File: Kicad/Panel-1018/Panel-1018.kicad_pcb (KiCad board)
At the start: 2 copper layers, 100 x 100 mm, 60 parts, among them P1 CONN2X3MOLEX, P10 CONN_6, P11 TST, P12 TST, P13 TST, P14 TST, P15 TST, P16 TST, P4 TST, P7 TST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

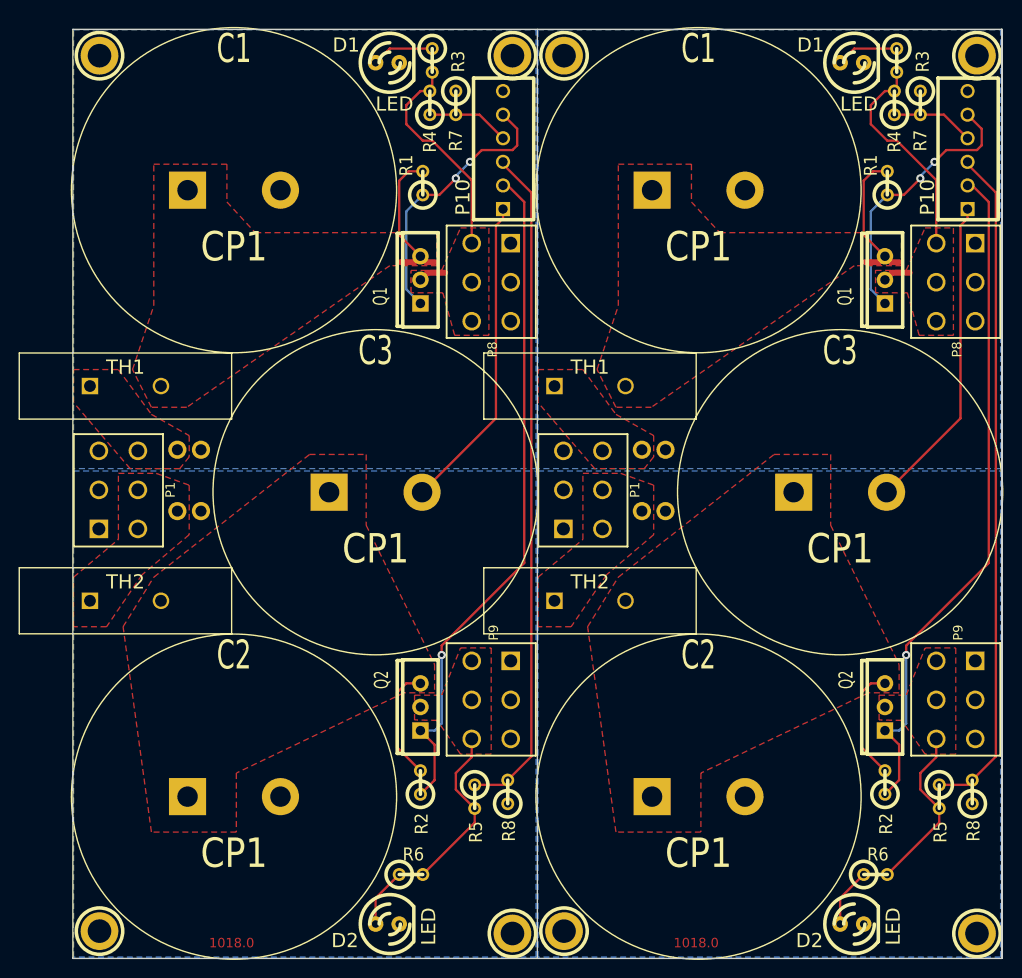
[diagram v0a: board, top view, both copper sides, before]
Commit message: Kicad:  Rename Panel-1018/Gerber/Gerber.zip to Panel-1018.zip.  Fix title on PCB legend.  Create Panel-1019 and Panel-1020 to panelize solenoid and incandescent planks.
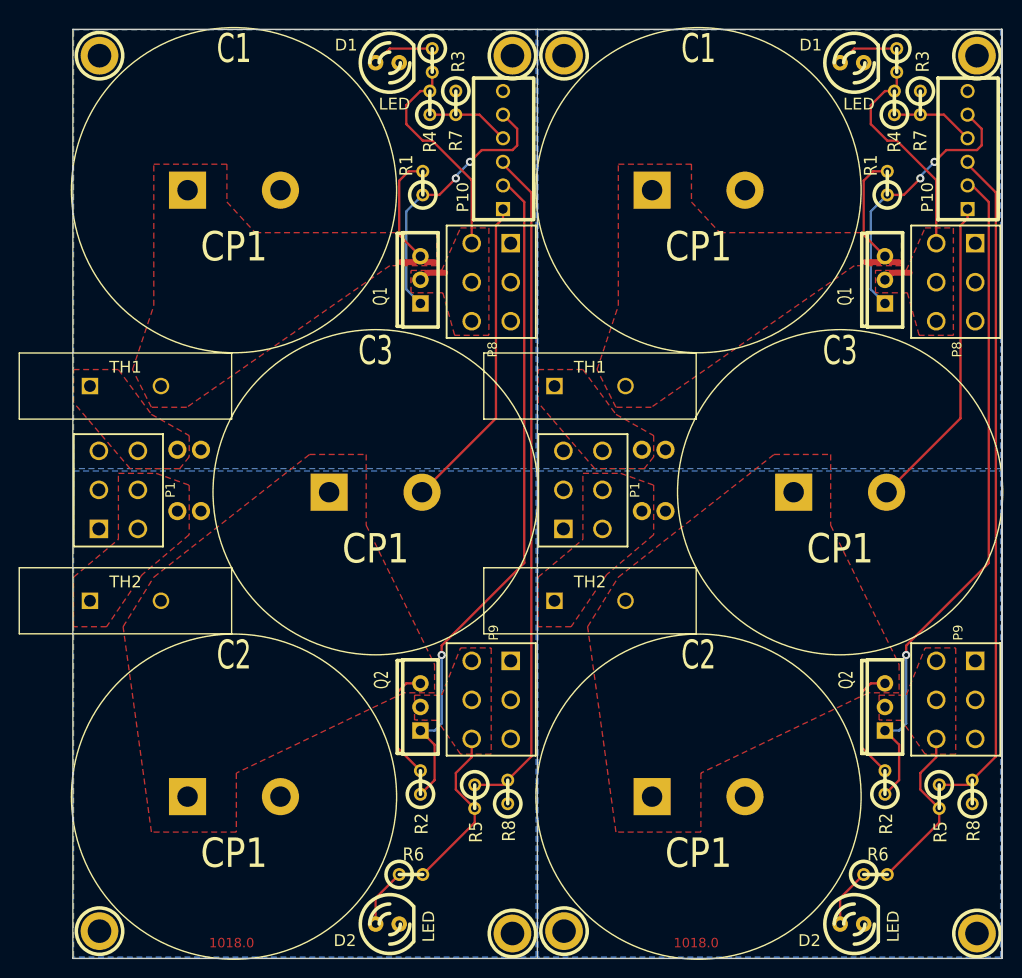
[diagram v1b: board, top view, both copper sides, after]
